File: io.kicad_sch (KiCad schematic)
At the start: 80 parts, among them IC16 MC1489, IC19 MC1488, IC23 MC1489, IC24 82C711 SIO, X7 24MHz

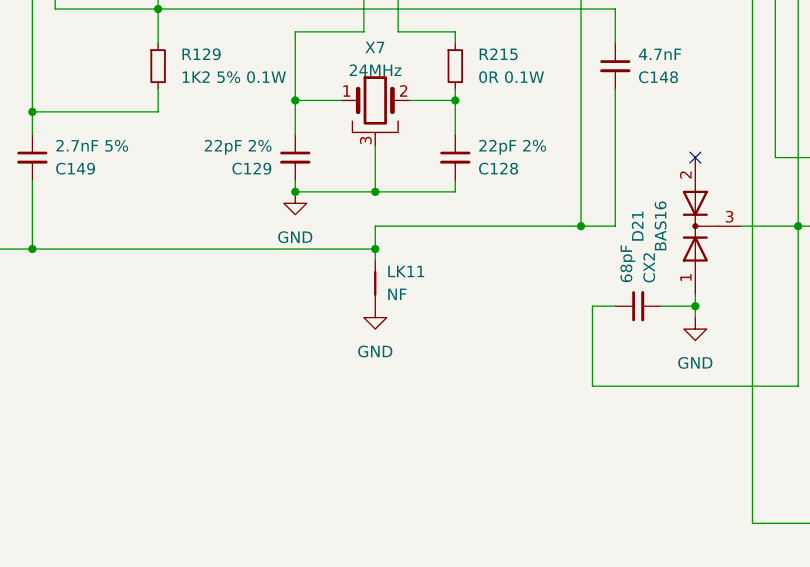
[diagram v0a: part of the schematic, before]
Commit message: turn LK12 into net tie, fix remaining DRC faults
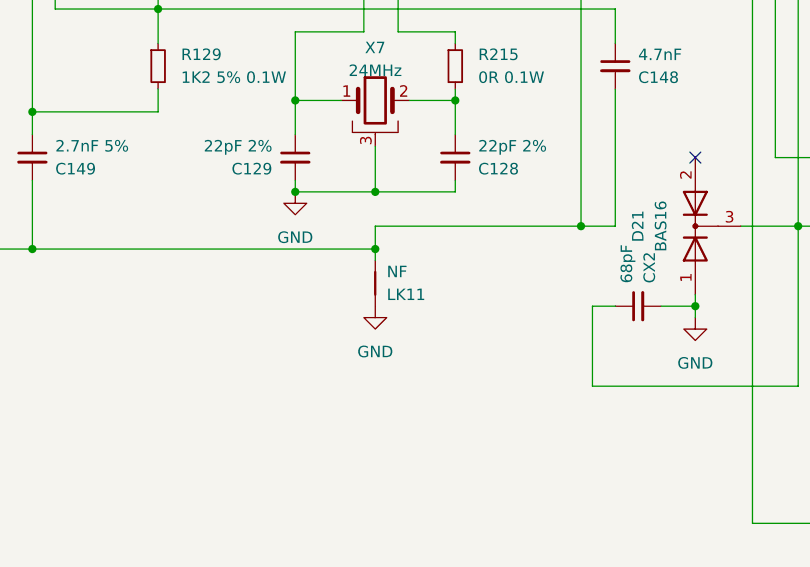
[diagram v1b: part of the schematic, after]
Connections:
- net GND: now also LK11.2; no longer LK11.1
- net at C148.2, C149.2, IC24.98 (Avss)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: now also LK11.1; no longer LK11.2
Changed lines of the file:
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@@
 		(lib_id "Device:NetTie_2")
 		(at 106.68 248.92 90)
+		(mirror x)
 		(unit 1)
 		(exclude_from_sim no)
@@
 		(on_board yes)
 		(dnp no)
-		(fields_autoplaced yes)
 		(property "Reference" "LK11"
-			(at 107.95 247.6499 90)
+			(at 107.95 250.1901 90)
 			(effects
 				(font
@@
 		)
 		(property "Value" "NF"
-			(at 107.95 250.1899 90)
+			(at 107.95 247.6501 90)
 			(effects
 				(font

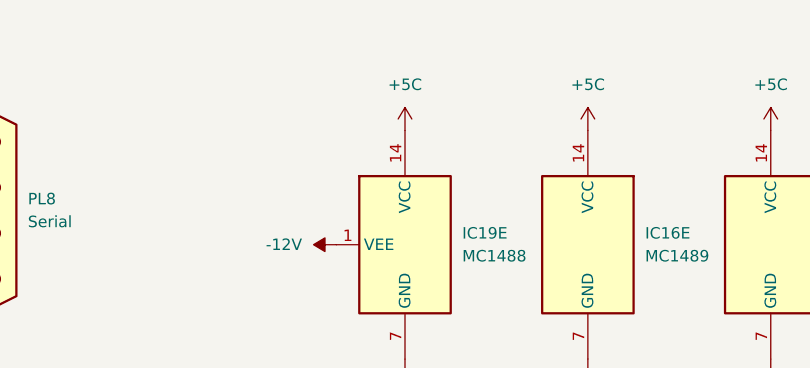
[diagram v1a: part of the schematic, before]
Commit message: add econet header
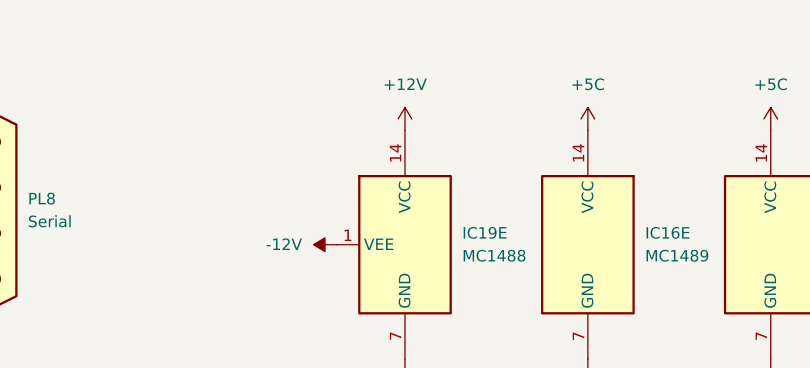
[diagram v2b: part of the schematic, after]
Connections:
- net +5C: no longer IC19.14 (VCC)
- new net +12V: IC19.14 (VCC)
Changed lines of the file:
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@@
+	)
+	(symbol
+		(lib_id "power:+12V")
+		(at 350.52 26.67 0)
+		(unit 1)
+		(exclude_from_sim no)
+		(in_bom yes)
+		(on_board yes)
+		(dnp no)
+		(fields_autoplaced yes)
+		(property "Reference" "#PWR0147"
+			(at 350.52 30.48 0)
+			(effects
+				(font
+					(size 1.27 1.27)
+				)
+				(hide yes)
+			)
+		)
+		(property "Value" "+12V"
+			(at 350.52 21.59 0)
+			(effects
+				(font
+					(size 1.27 1.27)
+				)
+			)
+		)
+		(property "Footprint" ""
+			(at 350.52 26.67 0)
+			(effects
+				(font
+					(size 1.27 1.27)
+				)
+				(hide yes)
+			)
+		)
+		(property "Datasheet" ""
+			(at 350.52 26.67 0)
+			(effects
+				(font
+					(size 1.27 1.27)
+				)
+				(hide yes)
+			)
+		)
+		(property "Description" "Power symbol creates a global label with name \"+12V\""
+			(at 350.52 26.67 0)
+			(effects
+				(font
+					(size 1.27 1.27)
+				)
+				(hide yes)
+			)
+		)
+		(pin "1"
+		)
+		(instances
+			(project "Acorn-A3010"
+				(path "/999882f3-94f8-4a89-9093-27a47d0cb289/b04534ef-c242-4ca8-9b8d-9d4b3e26f2f3"
+					(reference "#PWR0147")
+					(unit 1)
+				)
+			)
+		)
 	)
 	(symbol
@@
 					(unit 1)
 				)
-			)
-		)
-	)
-	(symbol
-		(lib_id "power:+5C")
-		(at 350.52 26.67 0)
-		(unit 1)
-		(exclude_from_sim no)
-		(in_bom yes)
-		(on_board yes)
-		(dnp no)
-		(fields_autoplaced yes)
-		(property "Reference" "#PWR0147"
-			(at 350.52 30.48 0)
-			(effects
-				(font
-					(size 1.27 1.27)
-				)
-				(hide yes)
-			)
-		)
-		(property "Value" "+5C"
-			(at 350.52 21.59 0)
-			(effects
-				(font
-					(size 1.27 1.27)
-				)
-			)
-		)
-		(property "Footprint" ""
-			(at 350.52 26.67 0)
-			(effects
-				(font
-					(size 1.27 1.27)
-				)
-				(hide yes)
-			)
-		)
-		(property "Datasheet" ""
-			(at 350.52 26.67 0)
-			(effects
-				(font
-					(size 1.27 1.27)
-				)
-				(hide yes)
-			)
-		)
-		(property "Description" "Power symbol creates a global label with name \"+5C\""
-			(at 350.52 26.67 0)
-			(effects
-				(font
-					(size 1.27 1.27)
-				)
-				(hide yes)
-			)
-		)
-		(pin "1"
-		)
-		(instances
-			(project "Acorn-A3010"
-				(path "/999882f3-94f8-4a89-9093-27a47d0cb289/b04534ef-c242-4ca8-9b8d-9d4b3e26f2f3"
-					(reference "#PWR0147")
-					(unit 1)
-				)

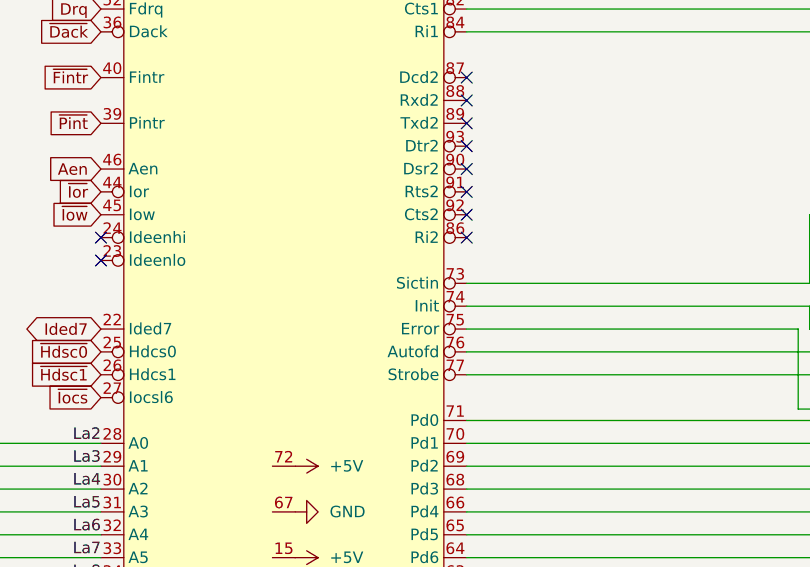
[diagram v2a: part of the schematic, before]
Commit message: fix rtc wiring
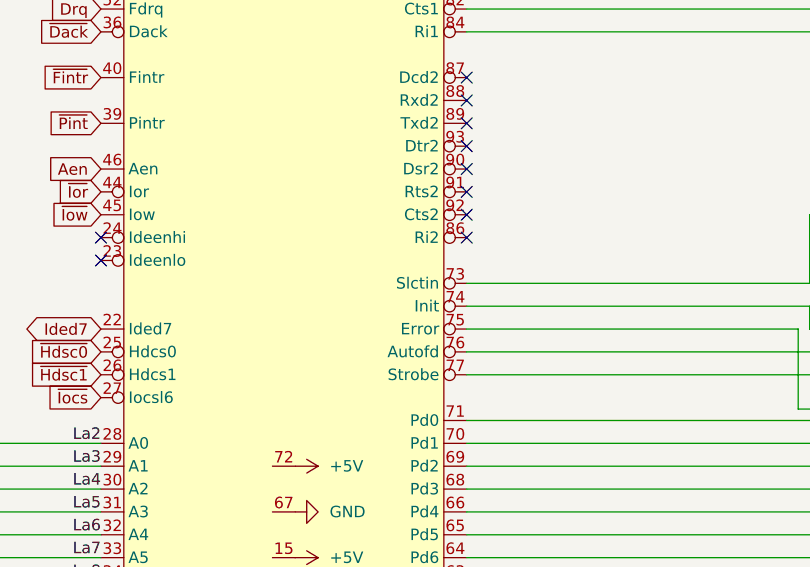
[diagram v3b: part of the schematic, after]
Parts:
- IC24: footprint Acorn:PQFP-100_14x20mm_P0.65mm -> Package_QFP:TQFP-100_14x14mm_P0.5mm
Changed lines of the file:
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@@
 			)
 		)
-		(property "Footprint" "Acorn:PQFP-100_14x20mm_P0.65mm"
+		(property "Footprint" "Package_QFP:TQFP-100_14x14mm_P0.5mm"
 			(at 106.68 120.65 0)
 			(effects

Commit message: fix deviant footprint for SuperIO
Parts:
- IC24: footprint Package_QFP:TQFP-100_14x14mm_P0.5mm -> Acorn:PQFP-100_14x20mm_P0.65mm
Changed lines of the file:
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@@
 			)
 		)
-		(property "Footprint" "Package_QFP:TQFP-100_14x14mm_P0.5mm"
+		(property "Footprint" "Acorn:PQFP-100_14x20mm_P0.65mm"
 			(at 106.68 120.65 0)
 			(effects

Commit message: adopt later issue 2 version of FDD index circuit
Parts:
- removed D21: BAS16, Package_TO_SOT_SMD:SOT-23-3, symbol Device:D_Dual_CommonCathode_AAK
- C75: renamed from CX2; footprint Capacitor_THT:C_Disc_D4.3mm_W1.9mm_P5.00mm -> Capacitor_SMD:C_0805_2012Metric
- R67: renamed from RX1; value 68R -> 82R; footprint Resistor_THT:R_Axial_DIN0204_L3.6mm_D1.6mm_P5.08mm_Horizontal -> Resistor_SMD:R_0805_2012Metric
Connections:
- net GND: now also C75.1; no longer C75.2
- net ~{Index}: now also C75.2; no longer C75.1, PL9.8 (Pin_8), R139.1, R67.2
- new net: PL9.8 (Pin_8), R139.1, R67.2
- no-connect marks 34 -> 33
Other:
- moved on the sheet: C75, R67
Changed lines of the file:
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@@
 	)
 	(junction
-		(at 250.19 242.57)
-		(diameter 0)
-		(color 0 0 0 0)
-	)
-	(junction
 		(at 217.17 87.63)
 		(diameter 0)
@@
 	)
 	(junction
-		(at 142.24 251.46)
-		(diameter 0)
-		(color 0 0 0 0)
-	)
-	(junction
 		(at 270.51 255.27)
 		(diameter 0)
@@
 	)
 	(junction
-		(at 245.11 242.57)
-		(diameter 0)
-		(color 0 0 0 0)
-	)
-	(junction
 		(at 270.51 252.73)
 		(diameter 0)
@@
 	)
 	(no_connect
-		(at 142.24 234.95)
-	)
-	(no_connect
 		(at 398.78 220.98)
 	)
@@
 		)
 	)
-	(wire
-		(pts
-			(xy 250.19 240.03) (xy 250.19 242.57)
-		)
-		(stroke
-			(width 0)
-			(type default)
-		)
-	)
 	(bus
 		(pts
@@
 	(wire
 		(pts
+			(xy 223.52 242.57) (xy 254 242.57)
+		)
+		(stroke
+			(width 0)
+			(type default)
+		)
+	)
+	(wire
+		(pts
 			(xy 203.2 107.95) (xy 203.2 115.57)
 		)
@@
 	(wire
 		(pts
+			(xy 207.01 242.57) (xy 223.52 242.57)
+		)
+		(stroke
+			(width 0)
+			(type default)
+		)
+	)
+	(wire
+		(pts
 			(xy 153.67 189.23) (xy 182.88 189.23)
 		)
@@
 	(wire
 		(pts
+			(xy 142.24 242.57) (xy 142.24 243.84)
+		)
+		(stroke
+			(width 0)
+			(type default)
+		)
+	)
+	(wire
+		(pts
 			(xy 38.1 181.61) (xy 38.1 186.69)
 		)
@@
 	(wire
 		(pts
-			(xy 142.24 252.73) (xy 142.24 251.46)
-		)
-		(stroke
-			(width 0)
-			(type default)
-		)
-	)
-	(wire
-		(pts
 			(xy 233.68 64.77) (xy 245.11 64.77)
 		)
@@
 	(wire
 		(pts
-			(xy 250.19 242.57) (xy 254 242.57)
-		)
-		(stroke
-			(width 0)
-			(type default)
-		)
-	)
-	(wire
-		(pts
 			(xy 52.07 184.15) (xy 87.63 184.15)
 		)
@@
 	(wire
 		(pts
-			(xy 153.67 260.35) (xy 130.81 260.35)
-		)
-		(stroke
-			(width 0)
-			(type default)
-		)
-	)
-	(wire
-		(pts
 			(xy 102.87 228.6) (xy 97.79 228.6)
 		)
@@
 	(wire
 		(pts
-			(xy 245.11 242.57) (xy 250.19 242.57)
-		)
-		(stroke
-			(width 0)
-			(type default)
-		)
-	)
-	(wire
-		(pts
 			(xy 270.51 237.49) (xy 270.51 240.03)
 		)
@@
 	(wire
 		(pts
-			(xy 245.11 240.03) (xy 245.11 242.57)
-		)
-		(stroke
-			(width 0)
-			(type default)
-		)
-	)
-	(wire
-		(pts
 			(xy 194.31 120.65) (xy 195.58 120.65)
 		)
@@
 	(wire
 		(pts
-			(xy 153.67 242.57) (xy 223.52 242.57)
+			(xy 153.67 242.57) (xy 201.93 242.57)
 		)
 		(stroke
@@
 	(wire
 		(pts
-			(xy 153.67 242.57) (xy 153.67 260.35)
-		)
-		(stroke
-			(width 0)
-			(type default)
-		)
-	)
-	(wire
-		(pts
 			(xy 168.91 123.19) (xy 168.91 120.65)
 		)
@@
 	(wire
 		(pts
-			(xy 142.24 251.46) (xy 142.24 250.19)
+			(xy 142.24 248.92) (xy 142.24 252.73)
 		)
 		(stroke
@@
 	(wire
 		(pts
+			(xy 142.24 242.57) (xy 153.67 242.57)
+		)
+		(stroke
+			(width 0)
+			(type default)
+		)
+	)
+	(wire
+		(pts
 			(xy 185.42 74.93) (xy 185.42 58.42)
 		)
@@
 		)
 	)
-	(wire
-		(pts
-			(xy 223.52 242.57) (xy 245.11 242.57)
-		)
-		(stroke
-			(width 0)
-			(type default)
-		)
-	)
 	(bus
 		(pts
@@
 	(wire
 		(pts
-			(xy 138.43 251.46) (xy 142.24 251.46)
-		)
-		(stroke
-			(width 0)
-			(type default)
-		)
-	)
-	(wire
-		(pts
 			(xy 128.27 62.23) (xy 172.72 62.23)
 		)
@@
 	(wire
 		(pts
-			(xy 147.32 242.57) (xy 153.67 242.57)
-		)
-		(stroke
-			(width 0)
-			(type default)
-		)
-	)
-	(wire
-		(pts
 			(xy 243.84 252.73) (xy 254 252.73)
 		)
@@
 	(wire
 		(pts
-			(xy 130.81 251.46) (xy 133.35 251.46)
-		)
-		(stroke
-			(width 0)
-			(type default)
-		)
-	)
-	(wire
-		(pts
 			(xy 179.07 273.05) (xy 254 273.05)
 		)
@@
 	(wire
 		(pts
-			(xy 130.81 260.35) (xy 130.81 251.46)
-		)
-		(stroke
-			(width 0)
-			(type default)
-		)
-	)
-	(wire
-		(pts
 			(xy 325.12 137.16) (xy 328.93 137.16)
 		)
@@
 	)
 	(symbol
-		(lib_id "Device:D_Dual_CommonCathode_AAK")
-		(at 142.24 242.57 90)
-		(unit 1)
-		(exclude_from_sim no)
-		(in_bom yes)
-		(on_board yes)
-		(dnp no)
-		(property "Reference" "D21"
-			(at 135.89 242.57 0)
-			(effects
-				(font
-					(size 1.27 1.27)
-				)
-			)
-		)
-		(property "Value" "BAS16"
-			(at 138.43 242.57 0)
-			(effects
-				(font
-					(size 1.27 1.27)
-				)
-			)
-		)
-		(property "Footprint" "Package_TO_SOT_SMD:SOT-23-3"
-			(at 142.24 242.57 0)
-			(effects
-				(font
-					(size 1.27 1.27)
-				)
-				(hide yes)
-			)
-		)
-		(property "Datasheet" "~"
-			(at 142.24 242.57 0)
-			(effects
-				(font
-					(size 1.27 1.27)
-				)
-				(hide yes)
-			)
-		)
-		(property "Description" "Dual diode, common cathode on pin 3"
-			(at 142.24 242.57 0)
-			(effects
-				(font
-					(size 1.27 1.27)
-				)
-				(hide yes)
-			)
-		)
-		(pin "1"
-		)
-		(pin "2"
-		)
-		(pin "3"
-		)
-		(instances
-			(project "Acorn-A3010"
-				(path "/999882f3-94f8-4a89-9093-27a47d0cb289/b04534ef-c242-4ca8-9b8d-9d4b3e26f2f3"
-					(reference "D21")
-					(unit 1)
-				)
-			)
-		)
-	)
-	(symbol
 		(lib_id "Device:C_Small")
 		(at 195.58 158.75 0)
@@
 	(symbol
 		(lib_id "Device:C_Small")
-		(at 135.89 251.46 90)
+		(at 142.24 246.38 0)
 		(mirror x)
 		(unit 1)
@@
 		(on_board yes)
 		(dnp no)
-		(property "Reference" "CX2"
-			(at 137.1665 248.92 0)
+		(property "Reference" "C75"
+			(at 139.7 245.1035 0)
 			(effects
 				(font
@@
 		)
 		(property "Value" "68pF"
-			(at 134.6265 248.92 0)
+			(at 139.7 247.6435 0)
 			(effects
 				(font
@@
 			)
 		)
-		(property "Footprint" "Capacitor_THT:C_Disc_D4.3mm_W1.9mm_P5.00mm"
-			(at 135.89 251.46 0)
+		(property "Footprint" "Capacitor_SMD:C_0805_2012Metric"
+			(at 142.24 246.38 0)
 			(effects
 				(font
@@
 		)
 		(property "Datasheet" "~"
-			(at 135.89 251.46 0)
+			(at 142.24 246.38 0)
 			(effects
 				(font
@@
 		)
 		(property "Description" "Unpolarized capacitor, small symbol"
-			(at 135.89 251.46 0)
+			(at 142.24 246.38 0)
 			(effects
 				(font
@@
 			(project "Acorn-A3010"
 				(path "/999882f3-94f8-4a89-9093-27a47d0cb289/b04534ef-c242-4ca8-9b8d-9d4b3e26f2f3"
-					(reference "CX2")
+					(reference "C75")
 					(unit 1)
 				)
@@
 	(symbol
 		(lib_id "Device:R_Small")
-		(at 247.65 240.03 90)
+		(at 204.47 242.57 90)
 		(unit 1)
 		(exclude_from_sim no)
 		(in_bom yes)
-		(on_board no)
+		(on_board yes)
 		(dnp no)
 		(fields_autoplaced yes)
-		(property "Reference" "RX1"
-			(at 247.65 234.95 90)
+		(property "Reference" "R67"
+			(at 204.47 237.49 90)
 			(effects
 				(font
@@
 			)
 		)
-		(property "Value" "68R"
-			(at 247.65 237.49 90)
+		(property "Value" "82R"
+			(at 204.47 240.03 90)
 			(effects
 				(font
@@
 			)
 		)
-		(property "Footprint" "Resistor_THT:R_Axial_DIN0204_L3.6mm_D1.6mm_P5.08mm_Horizontal"
-			(at 247.65 240.03 0)
+		(property "Footprint" "Resistor_SMD:R_0805_2012Metric"
+			(at 204.47 242.57 0)
 			(effects
 				(font
@@
 		)
 		(property "Datasheet" "~"
-			(at 247.65 240.03 0)
+			(at 204.47 242.57 0)
 			(effects
 				(font
@@
 		)
 		(property "Description" "Resistor, small symbol"
-			(at 247.65 240.03 0)
+			(at 204.47 242.57 0)
 			(effects
 				(font
@@
 			(project "Acorn-A3010"
 				(path "/999882f3-94f8-4a89-9093-27a47d0cb289/b04534ef-c242-4ca8-9b8d-9d4b3e26f2f3"
-					(reference "RX1")
+					(reference "R67")
 					(unit 1)
 				)

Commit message: reinstate D21
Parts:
- added D21: BAT, Package_TO_SOT_SMD:SOT-23-3, symbol Device:D_Dual_CommonCathode_AAK
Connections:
- net GND: now also D21.1 (A)
- net ~{Index}: now also D21.3 (K)
- no-connect marks 33 -> 34
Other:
- moved on the sheet: C75
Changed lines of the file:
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@@
 	)
 	(junction
+		(at 146.05 256.54)
+		(diameter 0)
+		(color 0 0 0 0)
+	)
+	(junction
 		(at 203.2 107.95)
 		(diameter 0)
@@
 	)
 	(junction
+		(at 146.05 248.92)
+		(diameter 0)
+		(color 0 0 0 0)
+	)
+	(junction
 		(at 227.33 275.59)
 		(diameter 0)
@@
 	)
 	(no_connect
+		(at 137.16 241.3)
+	)
+	(no_connect
 		(at 398.78 220.98)
 	)
@@
 	(wire
 		(pts
+			(xy 137.16 256.54) (xy 146.05 256.54)
+		)
+		(stroke
+			(width 0)
+			(type default)
+		)
+	)
+	(wire
+		(pts
 			(xy 270.51 260.35) (xy 270.51 262.89)
 		)
@@
 	(wire
 		(pts
+			(xy 153.67 248.92) (xy 153.67 242.57)
+		)
+		(stroke
+			(width 0)
+			(type default)
+		)
+	)
+	(wire
+		(pts
 			(xy 252.73 135.89) (xy 252.73 156.21)
 		)
@@
 	(wire
 		(pts
-			(xy 142.24 242.57) (xy 142.24 243.84)
-		)
-		(stroke
-			(width 0)
-			(type default)
-		)
-	)
-	(wire
-		(pts
 			(xy 38.1 181.61) (xy 38.1 186.69)
 		)
@@
 	(wire
 		(pts
+			(xy 146.05 256.54) (xy 146.05 254)
+		)
+		(stroke
+			(width 0)
+			(type default)
+		)
+	)
+	(wire
+		(pts
 			(xy 52.07 184.15) (xy 87.63 184.15)
 		)
@@
 	(wire
 		(pts
-			(xy 142.24 248.92) (xy 142.24 252.73)
-		)
-		(stroke
-			(width 0)
-			(type default)
-		)
-	)
-	(wire
-		(pts
 			(xy 247.65 133.35) (xy 193.04 133.35)
 		)
@@
 	(wire
 		(pts
+			(xy 146.05 259.08) (xy 146.05 256.54)
+		)
+		(stroke
+			(width 0)
+			(type default)
+		)
+	)
+	(wire
+		(pts
 			(xy 128.27 64.77) (xy 175.26 64.77)
 		)
@@
 	(wire
 		(pts
-			(xy 142.24 242.57) (xy 153.67 242.57)
+			(xy 142.24 248.92) (xy 146.05 248.92)
 		)
 		(stroke
@@
 	(wire
 		(pts
+			(xy 146.05 248.92) (xy 153.67 248.92)
+		)
+		(stroke
+			(width 0)
+			(type default)
+		)
+	)
+	(wire
+		(pts
 			(xy 270.51 265.43) (xy 270.51 267.97)
 		)
@@
 	)
 	(symbol
+		(lib_id "Device:D_Dual_CommonCathode_AAK")
+		(at 137.16 248.92 90)
+		(unit 1)
+		(exclude_from_sim no)
+		(in_bom yes)
+		(on_board yes)
+		(dnp no)
+		(property "Reference" "D21"
+			(at 130.81 248.92 0)
+			(effects
+				(font
+					(size 1.27 1.27)
+				)
+			)
+		)
+		(property "Value" "BAT"
+			(at 133.35 248.92 0)
+			(effects
+				(font
+					(size 1.27 1.27)
+				)
+			)
+		)
+		(property "Footprint" "Package_TO_SOT_SMD:SOT-23-3"
+			(at 137.16 248.92 0)
+			(effects
+				(font
+					(size 1.27 1.27)
+				)
+				(hide yes)
+			)
+		)
+		(property "Datasheet" "~"
+			(at 137.16 248.92 0)
+			(effects
+				(font
+					(size 1.27 1.27)
+				)
+				(hide yes)
+			)
+		)
+		(property "Description" "Dual diode, common cathode on pin 3"
+			(at 137.16 248.92 0)
+			(effects
+				(font
+					(size 1.27 1.27)
+				)
+				(hide yes)
+			)
+		)
+		(pin "1"
+		)
+		(pin "2"
+		)
+		(pin "3"
+		)
+		(instances
+			(project "Acorn-A3010"
+				(path "/999882f3-94f8-4a89-9093-27a47d0cb289/b04534ef-c242-4ca8-9b8d-9d4b3e26f2f3"
+					(reference "D21")
+					(unit 1)
+				)
+			)
+		)
+	)
+	(symbol
 		(lib_id "Device:C_Small")
 		(at 195.58 158.75 0)
@@
 	(symbol
 		(lib_id "Device:C_Small")
-		(at 142.24 246.38 0)
+		(at 146.05 251.46 0)
 		(mirror x)
 		(unit 1)
@@
 		(dnp no)
 		(property "Reference" "C75"
-			(at 139.7 245.1035 0)
+			(at 143.51 250.1835 0)
 			(effects
 				(font
@@
 		)
 		(property "Value" "68pF"
-			(at 139.7 247.6435 0)
+			(at 143.51 252.7235 0)
 			(effects
 				(font
@@
 		)
 		(property "Footprint" "Capacitor_SMD:C_0805_2012Metric"
-			(at 142.24 246.38 0)
+			(at 146.05 251.46 0)
 			(effects
 				(font
@@
 		)
 		(property "Datasheet" "~"
-			(at 142.24 246.38 0)
+			(at 146.05 251.46 0)
 			(effects
 				(font
@@
 		)
 		(property "Description" "Unpolarized capacitor, small symbol"
-			(at 142.24 246.38 0)
+			(at 146.05 251.46 0)
 			(effects
 				(font
@@
 	(symbol
 		(lib_id "power:GND")
-		(at 142.24 252.73 0)
+		(at 146.05 259.08 0)
 		(unit 1)
 		(exclude_from_sim no)
@@
 		(fields_autoplaced yes)
 		(property "Reference" "#PWR0154"
-			(at 142.24 259.08 0)
+			(at 146.05 265.43 0)
 			(effects
 				(font
@@
 		)
 		(property "Value" "GND"
-			(at 142.24 257.81 0)
+			(at 146.05 264.16 0)
 			(effects
 				(font
@@
 		)
 		(property "Footprint" ""
-			(at 142.24 252.73 0)
+			(at 146.05 259.08 0)
 			(effects
 				(font
@@
 		)
 		(property "Datasheet" ""
-			(at 142.24 252.73 0)
+			(at 146.05 259.08 0)
 			(effects
 				(font
@@
 		)
 		(property "Description" "Power symbol creates a global label with name \"GND\" , ground"
-			(at 142.24 252.73 0)
+			(at 146.05 259.08 0)
 			(effects
 				(font
